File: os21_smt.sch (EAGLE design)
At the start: 88 parts, among them IC1 LM1117-33, IC2 ENC28J60, K1 G5V1, K2 G5V1, K3 G5V1, T1 2N2222, T2 2N2222, T3 2N2222, T4 2N2222, U1 ATMEGA328P, X1 32.768kHz, X10 22-23-2031, X2 16MHz, X3 25MHz, X8 22-23-2031, X9 22-23-2031

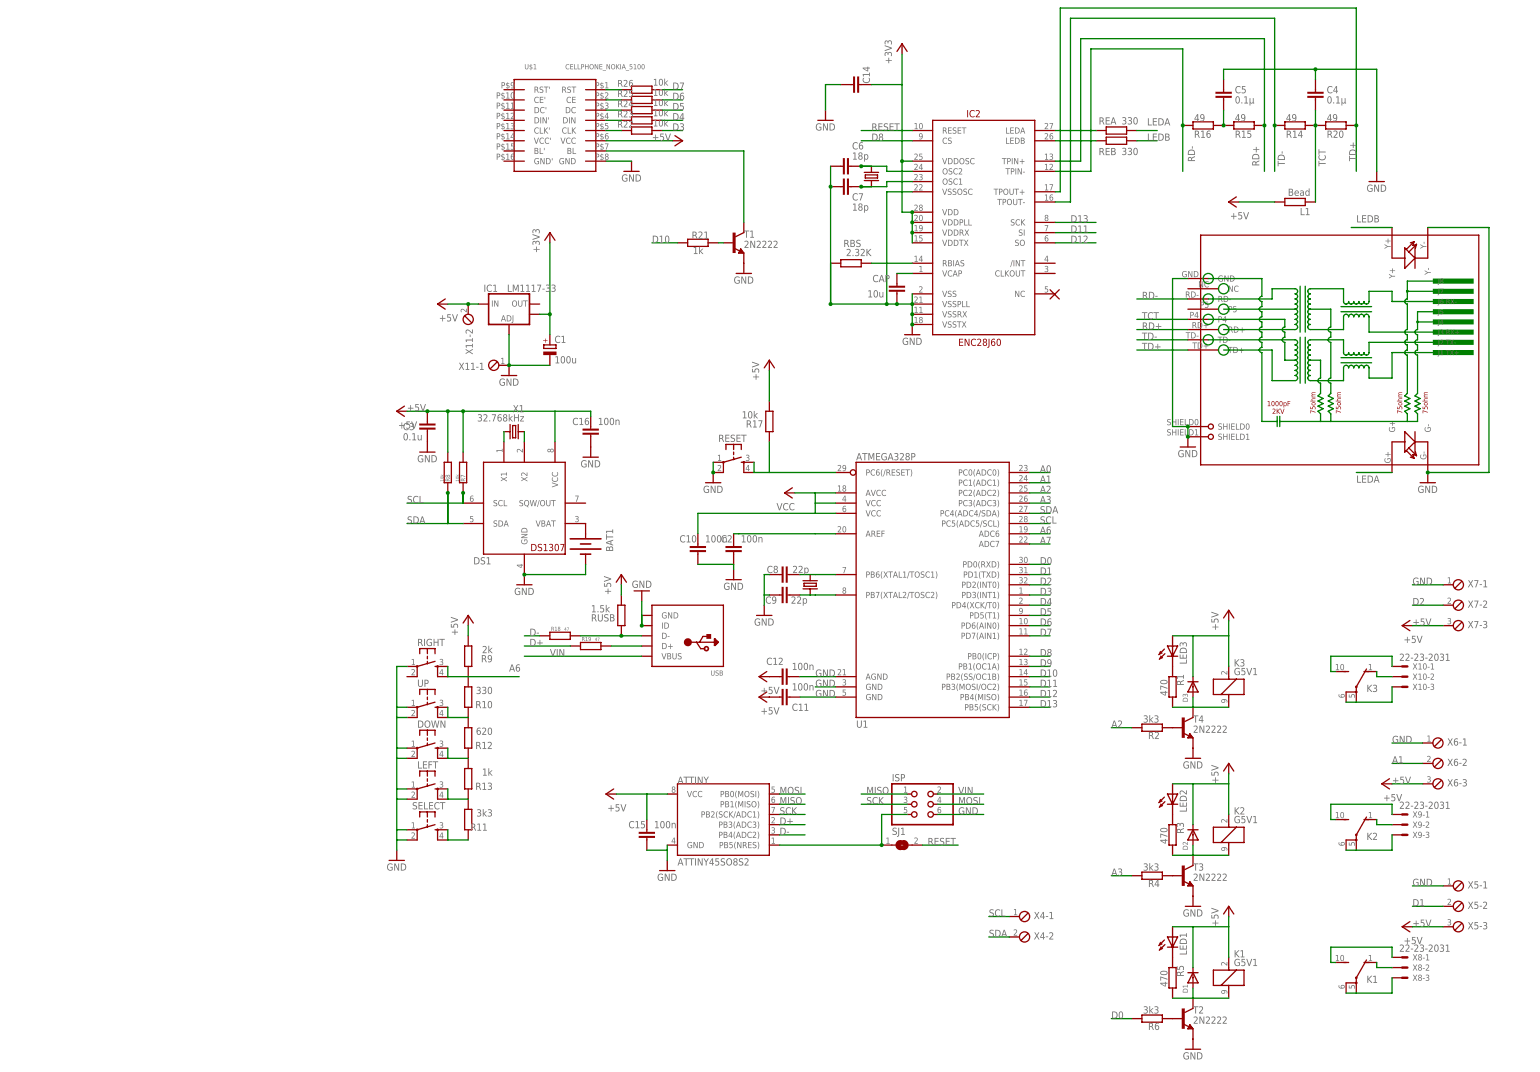
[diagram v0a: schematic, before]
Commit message: prijungta prie tinklo emoncms
veikiantis pvz
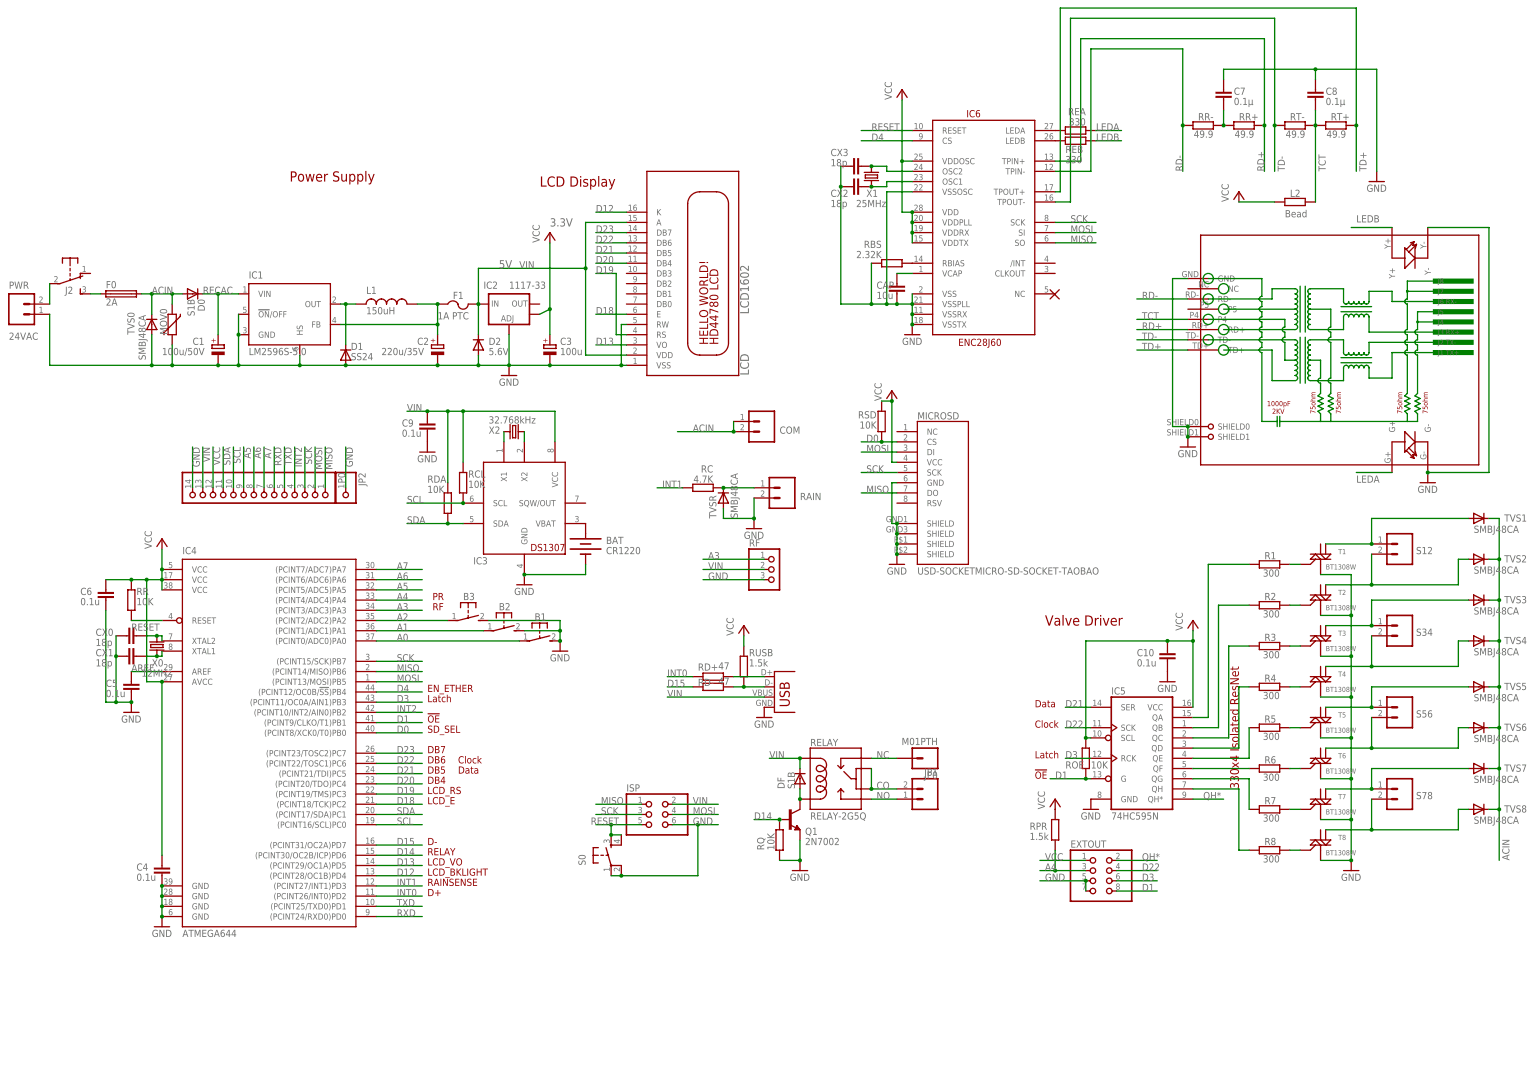
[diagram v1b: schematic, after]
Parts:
- removed ATTINY: ATTINY45SO8S2, SparkFun:ATTINY45SO8S2
- removed C11, C12, C14, C15, C16: 100n, resistor:C-EUC0805
- removed D3: (no value), adafruit:DIODEDO-1N4148
- removed DOWN, LEFT, RESET, RIGHT, SELECT, UP: (no value), SparkFun-Electromechanical:TAC_SWITCHPTH
- removed K1, K2, K3: G5V1, relay:G5V1
- removed LED1, LED2, LED3: (no value), adafruit:LEDSMT1206
- removed R10: 330, rcl:R-EU_R0805
- removed R11: 3k3, rcl:R-EU_R0805
- removed R12: 620, rcl:R-EU_R0805
- removed R13, R21: 1k, rcl:R-EU_R0805
- removed R17, R22, R23, R24, R25, R26: 10k, rcl:R-EU_R0805
- removed R18, R19: 47, rcl:R-EU_R0805
- removed R9: 2k, rcl:R-EU_R0805
- removed SJ1: (no value), jumper:SJ
- removed U$1: CELLPHONE_NOKIA_5100, DIY-Cellphone:CELLPHONE_NOKIA_5100
- removed U1: ATMEGA328P, SparkFun-DigitalIC:ATMEGA328_SMT
- removed X10, X8, X9: 22-23-2031, con-molex:22-23-2031
- removed X11, X4: (no value), con-phoenix-254:MPT2
- removed X3: 25MHz, SparkFun:CRYSTALHC49US
- removed X5, X6, X7: (no value), con-phoenix-254:MPT3
- added B1, B2, B3: (no value), adafruit:31-XX
- added COM, JP1, RAIN, S12, S34, S56, S78: (no value), SparkFun:M025MM-X
- added CX0, CX1, CX2, CX3: 18p, resistor:C-EUC0805
- added D0, DF: S1B, diode:DIODE-DO-214AC
- added EXTOUT: (no value), pinhead:PINHD-2X4
- added F0: 2A, fuse:FUSESHK20L
- added F1: 1A PTC, adafruit:PTCFUSE-1812
- added IC4: ATMEGA644, atmel:ATMEGA644A
- added IC5: 74HC595N, SparkFun:74LS595D
- added IC6: ENC28J60, SparkFun:ENC28J60SO28LONG
- added J2: EG1206, adafruit:EG1206
- added JP0: M01PTH, SparkFun:M01PTH
- added JP2: (no value), adafruit:PINHD-1X1CB
- added L2: Bead, rcl:R-EU_R0805
- added LCD: LCD1602, adafruit:HD44780LCDNOHOLE
- added MICROSD: USD-SOCKETMICRO-SD-SOCKET-TAOBAO, SparkFunNew:USD-SOCKETMICRO-SD-SOCKET-TAOBAO
- added MOV0: MOV, varistor:VARISTOR-5
- added P0: (no value), adafruit:PINHD-1X14-CB
- added PWR: 24VAC, SparkFun:M024MM-X
- added Q1: 2N7002, SparkFunNew:TRANSISTOR_NPNSOT23-3
- added RC: 4.7K, rcl:R-EU_R0805
- added RCL, RDA, ROE, RQ, RR, RSD: 10K, rcl:R-EU_R0805
- added RD+, RD-: 47, rcl:R-EU_R0805
- added RELAY: RELAY-2G5Q, SparkFunNew:RELAY-2G5Q
- added RF: (no value), pinhead:PINHD-1X3
- added RPR: 1.5k, rcl:R-EU_R0805
- added S0: (no value), SparkFunNew:TAC_SWITCHSMD
- added T5, T6, T7, T8: BT1308W, SparkFun:MAC97SOT223
- added TVS0, TVS1, TVS2, TVS3, TVS4, TVS5, TVS6, TVS7, TVS8, TVSR: SMBJ48CA, diode:DIODE-SMB
- added X0: 12MHz, SparkFun:CRYSTALHC49UV
- BAT: value (none) -> CR1220
- C1: value 100u -> 100u/50V; device resistor:CPOL-EUE2-5 -> resistor:CPOL-EUE3.5-8
- C10: value 100n -> 0.1u; device resistor:C-EUC0805 -> rcl:C-EUC0805
- C2: value 100n -> 220u/35V; device resistor:C-EUC0805 -> resistor:CPOL-EUE3.5-8
- C3: value 0.1u -> 100u; device rcl:C-EUC0805 -> resistor:CPOL-EUD
- C4, C5: value 0.1µ -> 0.1u; device resistor:C-EUC0805 -> rcl:C-EUC0805
- C6: value 18p -> 0.1u; device resistor:C-EUC0805 -> rcl:C-EUC0805
- C7: value 18p -> 0.1µ
- C8: value 22p -> 0.1µ
- C9: value 22p -> 0.1u; device resistor:C-EUC0805 -> rcl:C-EUC0805
- D1: value (none) -> SS24; device adafruit:DIODEDO-1N4148 -> diode:DIODE-SMB
- D2: value (none) -> 5.6V; device adafruit:DIODEDO-1N4148 -> diode:DIODE-MINIMELF
- IC1: value LM1117-33 -> LM2596S-5.0; device SparkFun:V_REG_LM1117SOT223 -> national-semiconductor:LM2596S
- IC2: value ENC28J60 -> 1117-33; device SparkFun-DigitalIC:ENC28J60 -> SparkFun:V_REG_LM1117SOT223
- L1: value Bead -> 150uH; device rcl:R-EU_R0805 -> SparkFunNew:INDUCTORPWR
- R1, R3, R5: value 470 -> 300
- R2, R4, R6: value 3k3 -> 300
- R7, R8: value 10k -> 300
- RR+, RR-, RT+, RT-: value 49 -> 49.9
- T1, T2, T3, T4: value 2N2222 -> BT1308W; device adafruit:2N2222 -> SparkFun:MAC97SOT223
- USB: value (none) -> USBPTH; device adafruit:USBMOLEX -> SparkFunNew:USBPTH
- X1: value 32.768kHz -> 25MHz; device crystal:CRYSTALTC26H -> SparkFun:CRYSTALHC49UV
- X2: value 16MHz -> 32.768kHz; device SparkFun:CRYSTALHC49US -> crystal:CRYSTALTC38H
- renumbered BAT1 to BAT, DS1 to IC3, R14 to RT-, R15 to RR+, R16 to RR-, R20 to RT+, RJ1 to RJ45
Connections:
- removed net +3V3: C1.+, C14.1, IC1.OUT@1, IC2.VDD, IC2.VDDOSC, IC2.VDDPLL, IC2.VDDRX, IC2.VDDTX
- removed net +5V: ATTINY.VCC, C11.2, C12.2, C15.1, C16.1, C3.1, D1.C, D2.C, D3.C, IC1.IN, IC3.VCC, K11.1, K21.1, K31.1, L1.2, LED1.A, LED2.A, R7.2, R8.2, U$1.VCC, X11-2.1, X5-3.1, X6-3.1, X7-3.1
- removed net D+: ATTINY.PB3(ADC3), R19.1
- removed net D-: ATTINY.PB4(ADC2), R18.1
- removed net D10: R21.2, U1.PB2(SS/OC1B)
- removed net D11: IC2.SI, U1.PB3(MOSI/OC2)
- removed net D2: U1.PD2(INT0), X7-2.1
- removed net D5: R24.2, U1.PD5(T1)
- removed net D6: R25.2, U1.PD6(AIN0)
- removed net D7: R26.2, U1.PD7(AIN1)
- removed net D8: IC2.CS, U1.PB0(ICP)
- removed net D9: U1.PB1(OC1A)
- removed net N$44: R21.1, T1.B
- removed net N$46: R17.1, RESET.3, RESET.4, U1.PC6(/RESET)
- removed net N$52: ATTINY.PB5(NRES), ISP.5, SJ1.1
- removed net V$: R26.1, U$1.RST
- new net A4: EXTOUT.3, IC4.(PCINT4/ADC4)PA4, RPR.1
- new net A5: IC4.(PCINT5/ADC5)PA5, P0.9
- new net ACIN: COM.1, COM.2, D0.A, F0.2, MOV0.1, TVS0.C, TVS1.C, TVS2.C, TVS3.C, TVS4.C, TVS5.C, TVS6.C, TVS7.C, TVS8.C
- new net AREF: C5.1, IC4.AREF
- new net CO: JP1.2, RELAY.5, RELAY.6
- new net D14: IC4.(PCINT30/OC2B/ICP)PD6, Q1.B, RQ.1
- new net D15: IC4.(PCINT31/OC2A)PD7, RD-.1
- new net D18: IC4.(PCINT18/TCK)PC2, LCD.E
- new net D19: IC4.(PCINT19/TMS)PC3, LCD.RS
- new net D20: IC4.(PCINT20/TDO)PC4, LCD.DB4
- new net D21: IC4.(PCINT21/TDI)PC5, IC5.SER, LCD.DB5
- new net D22: EXTOUT.4, IC4.(PCINT22/TOSC1)PC6, IC5.SCK, LCD.DB6
- new net D23: IC4.(PCINT23/TOSC2)PC7, LCD.DB7
- new net INT0: IC4.(PCINT26/INT0)PD2, RD+.1
- new net INT1: IC4.(PCINT27/INT1)PD3, RC.1
- new net INT2: IC4.(PCINT10/INT2/AIN0)PB2, P0.4
- new net N$10: IC5.QE, R5.2
- new net NC: JP0.1, RELAY.1
- new net NO: JP1.1, RELAY.10
- new net QH*: EXTOUT.2, IC5.QH*
- new net RECAC: C1.+, D0.C, IC1.VIN
- new net RXD: IC4.(PCINT24/RXD0)PD0, P0.6
- new net TXD: IC4.(PCINT25/TXD0)PD1, P0.5
- net A0: now also B1.P, IC4.(PCINT0/ADC0)PA0; no longer U1.PC0(ADC0)
- net A1: now also B2.P, IC4.(PCINT1/ADC1)PA1; no longer U1.PC1(ADC1), X6-2.1
- net A2: now also B3.P, IC4.(PCINT2/ADC2)PA2; no longer R2.2, U1.PC2(ADC2)
- net A3: now also IC4.(PCINT3/ADC3)PA3, RF.1; no longer R4.2, U1.PC3(ADC3)
- net A6: now also IC4.(PCINT6/ADC6)PA6, P0.8; no longer R10.2, R9.1, RIGHT.3, RIGHT.4, U1.ADC6
- net A7: now also IC4.(PCINT7/ADC7)PA7, P0.7; no longer U1.ADC7
- net D0: now also IC4.(PCINT8/XCK0/T0)PB0, MICROSD.CS, RSD.1; no longer R6.2, U1.PD0(RXD)
- net D1: now also EXTOUT.8, IC4.(PCINT9/CLKO/T1)PB1, IC5.G, ROE.1; no longer U1.PD1(TXD), X5-2.1
- net D12: now also IC4.(PCINT28/OC1B)PD4, LCD.K; no longer IC2.SO, U1.PB4(MISO)
- net D13: now also IC4.(PCINT29/OC1A)PD5, LCD.VO; no longer IC2.SCK, U1.PB5(SCK)
- net D3: now also EXTOUT.6, IC4.(PCINT11/OC0A/AIN1)PB3, IC5.RCK; no longer R22.2, U1.PD3(INT1)
- net D4: now also IC4.(PCINT12/OC0B/!SS!)PB4, IC6.CS; no longer R23.2, U1.PD4(XCK/T0)
- net GND: now also B1.S, B2.S, B3.S, C2.-, C3.-, C4.2, C5.2, C7.1, C9.2, CX0.2, CX1.2, CX2.2, CX3.2, D1.A, D2.A, EXTOUT.5, EXTOUT.7, IC1.!ON!/OFF, IC1.GND, IC1.HS, IC2.ADJ, IC4.GND, IC4.GND@1, IC4.GND@2, IC4.GND@3, IC5.GND, IC6.VSS, IC6.VSSOSC, IC6.VSSPLL, IC6.VSSRX, IC6.VSSTX, JP2.1, LCD.RW, LCD.VSS, MICROSD.GND, MICROSD.SHIELD@1, MICROSD.SHIELD@2, MICROSD.SHIELD@3, MICROSD.SHIELD@4, MOV0.2, P0.14, PWR.1, Q1.E, RAIN.2, RF.3, RQ.2, S0.1, S0.2, T1.M1, T2.M1, T3.M1, T4.M1, T5.M1, T6.M1, T7.M1, T8.M1, TVS0.A, TVSR.A; no longer ATTINY.GND, C11.1, C12.1, C14.2, C15.2, C16.2, C2.2, C3.2, C4.1, C5.1, C7.2, C9.1, DOWN.1, DOWN.2, IC1.ADJ, IC2.VSS, IC2.VSSOSC, IC2.VSSPLL, IC2.VSSRX, IC2.VSSTX, LEFT.1, LEFT.2, RESET.1, RESET.2, RIGHT.1, SELECT.1, SELECT.2, T1.E, T2.E, T3.E, T4.E, U$1.GND, U1.AGND, U1.GND@1, U1.GND@2, UP.1, UP.2, USB.ID, X11-1.1, X5-1.1, X6-1.1, X7-1.1
- net MISO: now also IC4.(PCINT14/MISO)PB6, IC6.SO, MICROSD.DO, P0.1; no longer ATTINY.PB1(MISO)
- net MOSI: now also IC4.(PCINT13/MOSI)PB5, IC6.SI, MICROSD.DI, P0.2; no longer ATTINY.PB0(MOSI)
- net N$1: now also F0.1, J2.S; no longer LEFT.3, LEFT.4, R11.2, R13.1
- net N$11: now also IC5.QD, R4.2; no longer D1.A, K11.2, R5.2, T2.C
- net N$12: now also IC5.QC, R3.2; no longer D3.A, K31.2, R1.2, T4.C
- net N$13: now also IC5.QB, R2.2; no longer R2.1, T4.B
- net N$14: now also IC5.QA, R1.2; no longer K22.S, X9-1.S
- net N$15: now also CX0.1, IC4.XTAL2, X0.2; no longer K12.S, X8-1.S
- net N$16: now also S12.1, T1.M2-4, TVS1.A; no longer K32.S, X10-1.S
- net N$17: now also S12.2, T2.M2-4, TVS2.A; no longer R6.1, T2.B
- net N$18: now also S34.1, T3.M2-4, TVS3.A; no longer R11.1, SELECT.3, SELECT.4
- net N$19: now also CX1.1, IC4.XTAL1, X0.1; no longer K32.P, K32.P@1, X10-3.S
- net N$2: now also C2.+, F1.1, IC1.FB, L1.2; no longer D2.A, K21.2, R3.2, T3.C
- net N$20: now also S34.2, T4.M2-4, TVS4.A; no longer K32.O, X10-2.S
- net N$21: now also T1.G; no longer LED3.C
- net N$22: now also S56.1, T5.M2-4, TVS5.A; no longer R22.1, U$1.CLK
- net N$23: now also S56.2, T6.M2-4, TVS6.A; no longer R25.1, U$1.CE
- net N$24: now also S78.1, T7.M2-4, TVS7.A; no longer R24.1, U$1.DC
- net N$25: now also S78.2, T8.M2-4, TVS8.A; no longer R23.1, U$1.DIN
- net N$26: now also R2.1, T2.G; no longer T1.C, U$1.BL
- net N$27: now also R3.1, T3.G; no longer LED3.A
- net N$28: now also R4.1, T4.G; no longer K12.P, K12.P@1, X8-3.S
- net N$29: now also R5.1, T5.G; no longer K12.O, X8-2.S
- net N$3: now also RAIN.1, RC.2, TVSR.C; no longer R4.1, T3.B
- net N$30: now also X2.1; no longer X1.1
- net N$31: now also R6.1, T6.G; no longer LED1.C, R5.1
- net N$32: now also DF.A, Q1.C, RELAY.9; no longer C9.2, U1.PB7(XTAL2/TOSC2), X2.1
- net N$33: now also R7.1, T7.G; no longer C8.2, U1.PB6(XTAL1/TOSC1), X2.2
- net N$34: now also IC6.LEDA; no longer IC2.LEDA
- net N$35: now also R8.1, T8.G; no longer C2.1, U1.AREF
- net N$37: now also IC6.LEDB; no longer IC2.LEDB
- net N$38: now also RD+.2; no longer R19.2
- net N$39: now also IC6.VCAP; no longer IC2.VCAP
- net N$4: now also IC5.QF, R6.2; no longer K22.P, K22.P@1, X9-3.S
- net N$41: now also CX3.1, IC6.OSC2, X1.2; no longer C6.1, IC2.OSC2, X3.2
- net N$42: now also CX2.1, IC6.OSC1, X1.1; no longer C7.1, IC2.OSC1, X3.1
- net N$45: now also RD-.2; no longer R18.2
- net N$5: now also IC5.QG, R7.2; no longer K22.O, X9-2.S
- net N$54: now also C7.2, RR+.2, RR-.1; no longer C5.2, RR+.1, RR-.2
- net N$59: now also IC6.RBIAS; no longer IC2.RBIAS
- net N$6: now also J2.P, PWR.2; no longer DOWN.3, DOWN.4, R12.1, R13.2
- net N$7: now also IC5.QH, R8.2; no longer LED2.C, R3.1
- net N$8: now also X2.2; no longer X1.2
- net N$9: now also D1.C, IC1.OUT, L1.1; no longer R10.1, R12.2, UP.3, UP.4
- net RD+: now also IC6.TPIN+, RR+.1; no longer IC2.TPIN+, RR+.2
- net RD-: now also IC6.TPIN-, RR-.2; no longer IC2.TPIN-, RR-.1
- net RESET: now also IC4.RESET, IC6.RESET, ISP.5, RR.1, S0.3, S0.4; no longer IC2.RESET, SJ1.2
- net SCK: now also IC4.(PCINT15/SCK)PB7, IC6.SCK, MICROSD.SCK, P0.3; no longer ATTINY.PB2(SCK/ADC1)
- net SCL: now also IC4.(PCINT16/SCL)PC0, P0.10, RCL.1; no longer R7.1, U1.PC5(ADC5/SCL)
- net SDA: now also IC4.(PCINT17/SDA)PC1, P0.11, RDA.1; no longer R8.1, U1.PC4(ADC4/SDA)
- net TCT: now also C8.2, L2.1, RT+.2, RT-.1; no longer C4.2, L1.1, RT+.1, RT-.2
- net TD+: now also IC6.TPOUT+, RT+.1; no longer IC2.TPOUT+, RT+.2
- net TD-: now also IC6.TPOUT-, RT-.2; no longer IC2.TPOUT-, RT-.1
- net VCC: now also C3.+, C4.1, C6.1, EXTOUT.1, IC2.OUT@1, IC4.AVCC, IC4.VCC, IC4.VCC@1, IC4.VCC@2, IC5.SCL, IC5.VCC, IC6.VDD, IC6.VDDOSC, IC6.VDDPLL, IC6.VDDRX, IC6.VDDTX, L2.2, MICROSD.VCC, P0.12, ROE.2, RPR.2, RR.2, RSD.2; no longer R17.2, R9.2, U1.AVCC, U1.VCC@1, U1.VCC@2
- net VIN: now also C9.1, D2.C, DF.C, F1.2, IC2.IN, IC3.VCC, LCD.A, LCD.VDD, P0.13, RCL.2, RDA.2, RELAY.2, RF.2
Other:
- note added: "!OE"
- note added: "3.3V"
- note added: "330x4 Isolated ResNet"
- note added: "5V"
- note added: "Clock"
- note added: "D+"
- note added: "D-"
- note added: "DB4"
- note added: "DB5"
- note added: "DB6"
- note added: "DB7"
- note added: "Data"
- note added: "EN_ETHER"
- note added: "LCD Display"
- note added: "LCD_BKLIGHT"
- note added: "LCD_E"
- note added: "LCD_RS"
- note added: "LCD_VO"
- note added: "Latch"
- note added: "PR"
- note added: "Power Supply"
- note added: "RAINSENSE"
- note added: "RELAY"
- note added: "RF"
- note added: "SD_SEL"
- note added: "Valve Driver"
- moved on the sheet: C1, C10, C4, C5, C6, C7, C8, C9, D1, D2, ISP, R1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
